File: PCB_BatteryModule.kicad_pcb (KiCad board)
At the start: 2 copper layers, 103.2 x 117 mm, 90 parts, among them J1 Interconnect A, J2 Interconnect B, J3 Debug, J4 Button/Status, J5 Barrel_Jack, Q1 IRF7406, Q2 IRF7303, Q3 IRF7303, Q4 IRF7309, SW1 SW_Push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

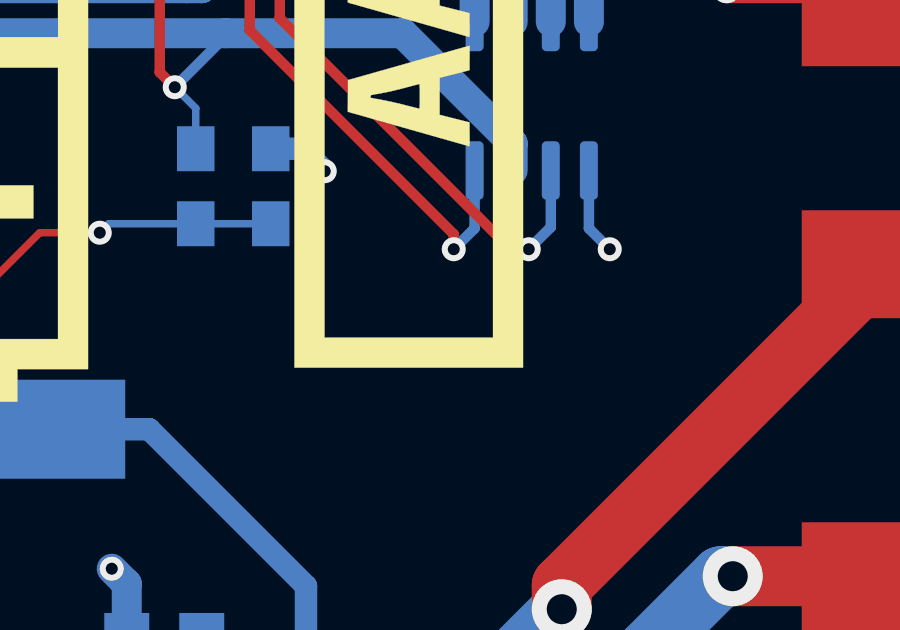
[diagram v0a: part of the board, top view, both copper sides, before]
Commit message: Add a pull-down resistor to the charger n-channel mosfet
Adding a pull-down resistor to the gate of the n-channel mosfet
prevents current from flowing through it when there is no charger voltage.
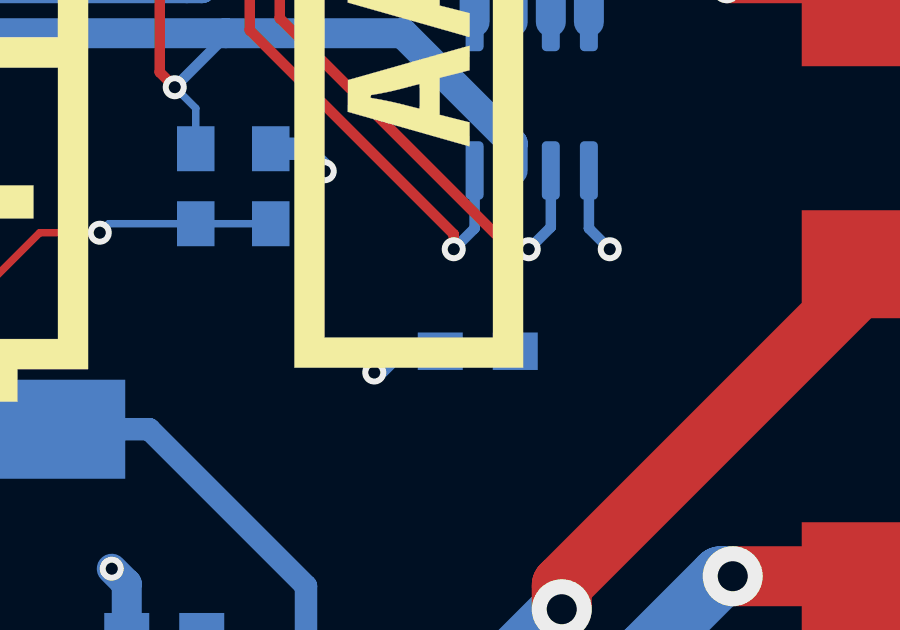
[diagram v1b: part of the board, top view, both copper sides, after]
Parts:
- added R18: 380K, PCB_BatteryModule:C_0805_HandSoldering, B.Cu at (172.2, 70.9)
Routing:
- net Net-(Q4-Pad2): track 26.0 -> 29.6 mm
- net -BATT: track 190.3 -> 192.8 mm, vias 43 -> 44

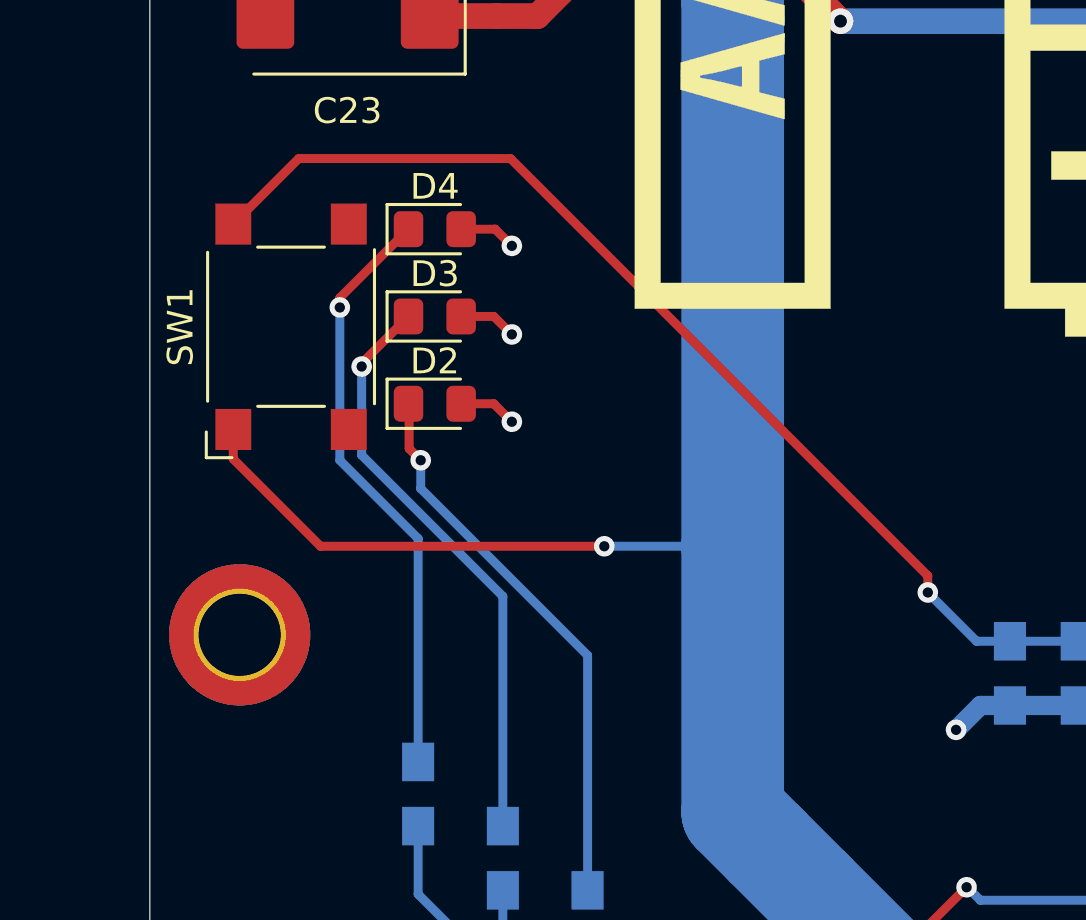
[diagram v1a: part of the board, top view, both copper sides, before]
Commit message: Use the correct footprint for the button
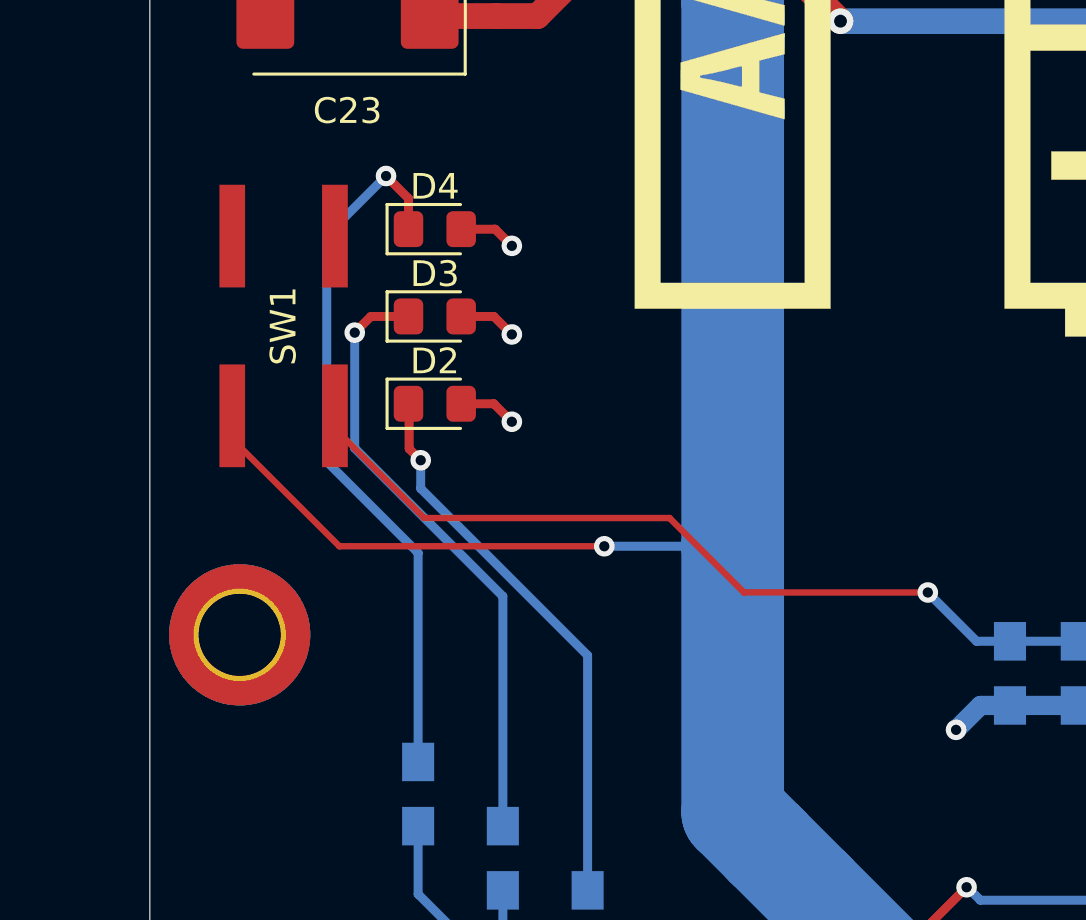
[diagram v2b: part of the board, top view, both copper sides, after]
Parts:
- SW1: footprint Button_Switch_SMD:SW_SPST_Omron_B3FS-100xP -> PCB_BatteryModule:CK_Switch_KSC_Series
- moved SW1 0.29 mm to (94.5, 72.2)
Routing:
- net Net-(J4-Pad9): track 98.2 -> 88.5 mm
- net Net-(D4-Pad1): track 23.1 -> 27.7 mm
- net Net-(D3-Pad1): track 22.9 -> 24.0 mm

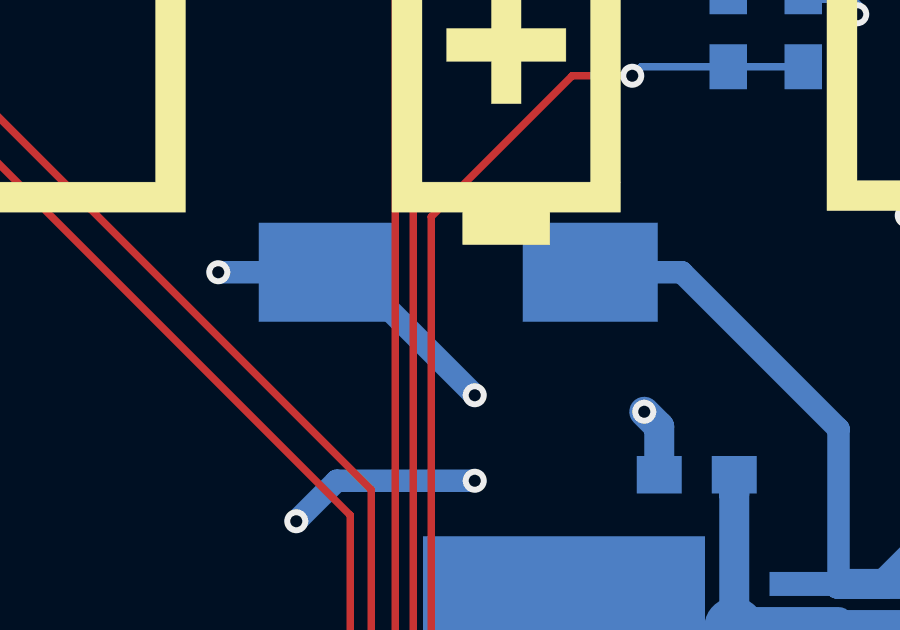
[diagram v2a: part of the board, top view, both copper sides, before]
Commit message: Change the D1 footprint to be regular SMC one instead of the handsoldering version
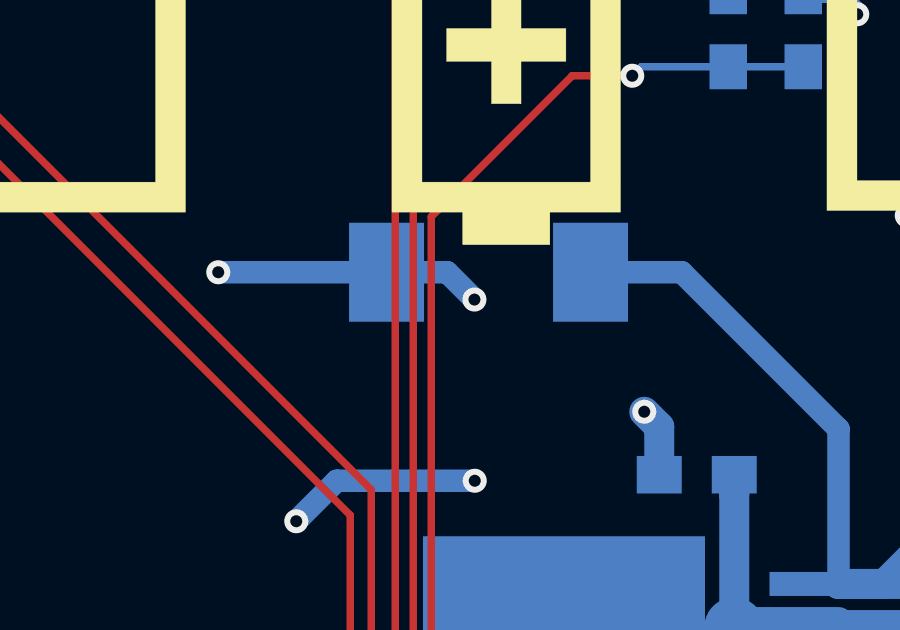
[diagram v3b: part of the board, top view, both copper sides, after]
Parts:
- D1: footprint Diodes_SMD:D_SMC_Handsoldering -> Diode_SMD:D_SMC
- moved D1 1.01 mm to (154.8, 73.5)
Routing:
- net -BATT: track 192.8 -> 191.5 mm

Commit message: Switch out the old logo to the new one and update the partnumber
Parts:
- removed the G*** at (94.2, 95.5)
- added G***: LOGO, PCB_BatteryModule:Text_KnektiumLogo_8mm_SolderMask, F.Cu at (94.8, 95.3)
- moved G*** 0.42 mm to (103.0, 63.3)
